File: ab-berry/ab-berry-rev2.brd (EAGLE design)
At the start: 58.4 x 61 mm, 66 parts, among them IC1 STM32F302RCT6, U1 LM1117MPX-3.3/NOPB or AP2114H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

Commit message: wip
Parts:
- removed STM32F072CBT6: STM32F072-LQFP48, stm32f0:LQFP48
- added R23, R24: 22, microbuilder:0603
- added X1: (no value), keves:TE-292304-1
- moved IC1 46.0 mm to (14.7, 33.4), flipped to the bottom
- moved C22 45.4 mm to (6.86, 29.8), flipped to the bottom, turned to 90 degrees
- moved R5 34.8 mm to (-9.14, 52.3)
- moved LED1 34.7 mm to (-9.02, 48.5)
- moved LED2 29.6 mm to (-7.37, 17.3)
- moved R6 29.1 mm to (-9.40, 13.1)
- moved R1 28.9 mm to (-10.8, 33.4)
- moved JP3 26.2 mm to (55.1, 50.0), turned to 90 degrees
- moved C12 15.3 mm to (18.4, 19.7), turned to 180 degrees
- moved C1 15.2 mm to (22.7, 30.1), turned to 90 degrees
- moved C13 14.1 mm to (14.9, 19.7), turned to 180 degrees
- moved C3 13.1 mm to (7.24, 39.0), turned to 270 degrees
- moved C6 11.9 mm to (21.0, 26.9)
- moved C5 10.8 mm to (10.3, 23.2), turned to 0 degrees
- moved U$36 10.5 mm to (16.6, 22.6), turned to 180 degrees
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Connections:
- new net N$18: R23.2, X1.2
- new net N$19: R24.2, X1.3
- new net SPI1_SCK: IC1.55, LCD2.CLK
- new net USB_DM: IC1.44, R23.1
- new net USB_DP: IC1.45, R24.1
- net 5.0V: now also X1.1
- net BTN_USR: now also IC1.2; no longer STM32F072CBT6.2
- net CAN_RX: now also IC1.61; no longer STM32F072CBT6.32
- net CAN_TX: now also IC1.62; no longer STM32F072CBT6.33
- net DBG_RX: no longer STM32F072CBT6.31
- net DBG_TX: no longer STM32F072CBT6.30
- net GND: now also X1.4
- net LCD_CS1: now also IC1.52; no longer STM32F072CBT6.20
- net LCD_CS2: now also IC1.53; no longer STM32F072CBT6.19
- net LCD_DC: now also IC1.59; no longer STM32F072CBT6.14
- net LCD_RST: now also IC1.58; no longer STM32F072CBT6.13
- net N$6: no longer STM32F072CBT6.18
- net N$8: now also IC1.5; no longer STM32F072CBT6.5
- net N$9: now also IC1.6; no longer STM32F072CBT6.6
- net ROT1_A: no longer STM32F072CBT6.27
- net ROT1_B: no longer STM32F072CBT6.28
- net ROT1_SW: no longer STM32F072CBT6.25
- net ROT2_A: no longer STM32F072CBT6.40
- net ROT2_B: no longer STM32F072CBT6.41
- net ROT2_SW: no longer STM32F072CBT6.39
- net ROT3_A: no longer STM32F072CBT6.43
- net ROT3_B: no longer STM32F072CBT6.45
- net ROT3_SW: no longer STM32F072CBT6.42
- net ROT4_A: no longer STM32F072CBT6.26
- net ROT4_B: no longer STM32F072CBT6.22
- net ROT4_SW: no longer STM32F072CBT6.21
- net SPI1_CLK: no longer LCD2.CLK, STM32F072CBT6.15
- net SPI1_MOSI: now also IC1.57; no longer STM32F072CBT6.17
- net SWCLK: no longer STM32F072CBT6.37
- net SWDIO: no longer STM32F072CBT6.34
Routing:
- net ROT4_A: track 54.1 -> 2.30 mm, vias 4 -> 0
- net ROT3_SW: track 46.7 -> 0.00 mm, vias 1 -> 0
- net SPI1_CLK: track 45.8 -> 0.00 mm, vias 1 -> 0
- net ROT3_B: track 44.7 -> 1.98 mm, vias 2 -> 0
- net ROT1_B: track 37.2 -> 2.12 mm, vias 4 -> 0
- net ROT1_A: track 35.3 -> 2.04 mm, vias 4 -> 0
- net ROT3_A: track 34.2 -> 1.98 mm, vias 2 -> 0
- net ROT2_SW: track 27.5 -> 0.00 mm, vias 1 -> 0
- net DBG_TX: track 24.8 -> 0.00 mm, vias 2 -> 0
- net DBG_RX: track 24.5 -> 0.00 mm, vias 2 -> 0
- net ROT1_SW: track 19.6 -> 0.00 mm, vias 3 -> 0
- net ROT4_B: track 54.2 -> 35.6 mm
- net ROT4_SW: track 41.3 -> 23.4 mm
- net LCD_CS1: track 48.5 -> 31.3 mm
- net SWDIO: track 16.8 -> 0.00 mm
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
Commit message: wip
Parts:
- moved R5 60.2 mm to (49.5, 39.0)
- moved LED1 60.0 mm to (49.5, 35.3)
- moved R1 35.6 mm to (24.6, 29.8), turned to 90 degrees
- moved R6 30.5 mm to (5.84, 39.5), turned to 180 degrees
- moved LED2 24.3 mm to (2.41, 39.5), turned to 270 degrees
- moved C3 1.80 mm to (5.97, 37.7), turned to 180 degrees
- moved C1 1.42 mm to (22.5, 28.7)
- moved C6 1.14 mm to (20.4, 25.9)
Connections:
- net DBG_RX: now also IC1.30
- net DBG_TX: now also IC1.29
- net N$6: now also IC1.33
- net ROT1_A: now also IC1.16
- net ROT1_B: now also IC1.15
- net ROT1_SW: now also IC1.14
- net ROT2_A: now also IC1.38
- net ROT2_B: now also IC1.40
- net ROT2_SW: now also IC1.39
- net ROT3_A: now also IC1.42
- net ROT3_B: now also IC1.43
- net ROT3_SW: now also IC1.41
- net ROT4_A: now also IC1.10
- net ROT4_B: now also IC1.9
- net ROT4_SW: now also IC1.8

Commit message: wip
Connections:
- removed net SPI1_CLK: LCD1.CLK
- net SPI1_SCK: now also LCD1.CLK
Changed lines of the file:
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@@
 <wire x1="20.482" y1="32.651" x2="26.84" y2="27.94" width="0" layer="19" extent="16-16"/>
-</signal>
-<signal name="SPI1_CLK">
-<contactref element="LCD1" pad="CLK"/>
 </signal>
 <signal name="LCD_CS2">
@@
 <contactref element="IC1" pad="55"/>
 <contactref element="LCD2" pad="CLK"/>
+<contactref element="LCD1" pad="CLK"/>
+<wire x1="26.84" y1="33.02" x2="56.304" y2="33.02" width="0" layer="19" extent="1-1"/>
 <wire x1="20.482" y1="34.151" x2="26.84" y2="33.02" width="0" layer="19" extent="16-16"/>
 </signal>

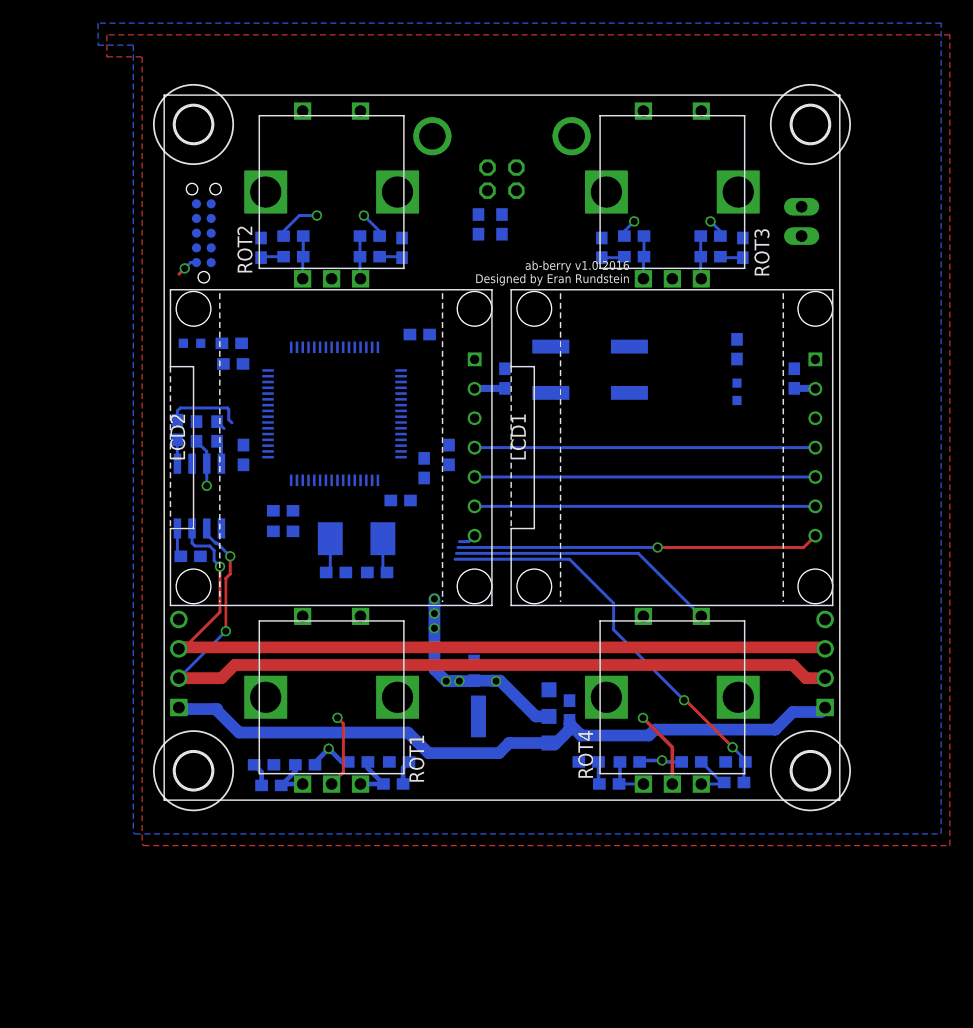
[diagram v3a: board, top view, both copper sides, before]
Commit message: switch ab-berry-rev2 to STM32F303CCT6
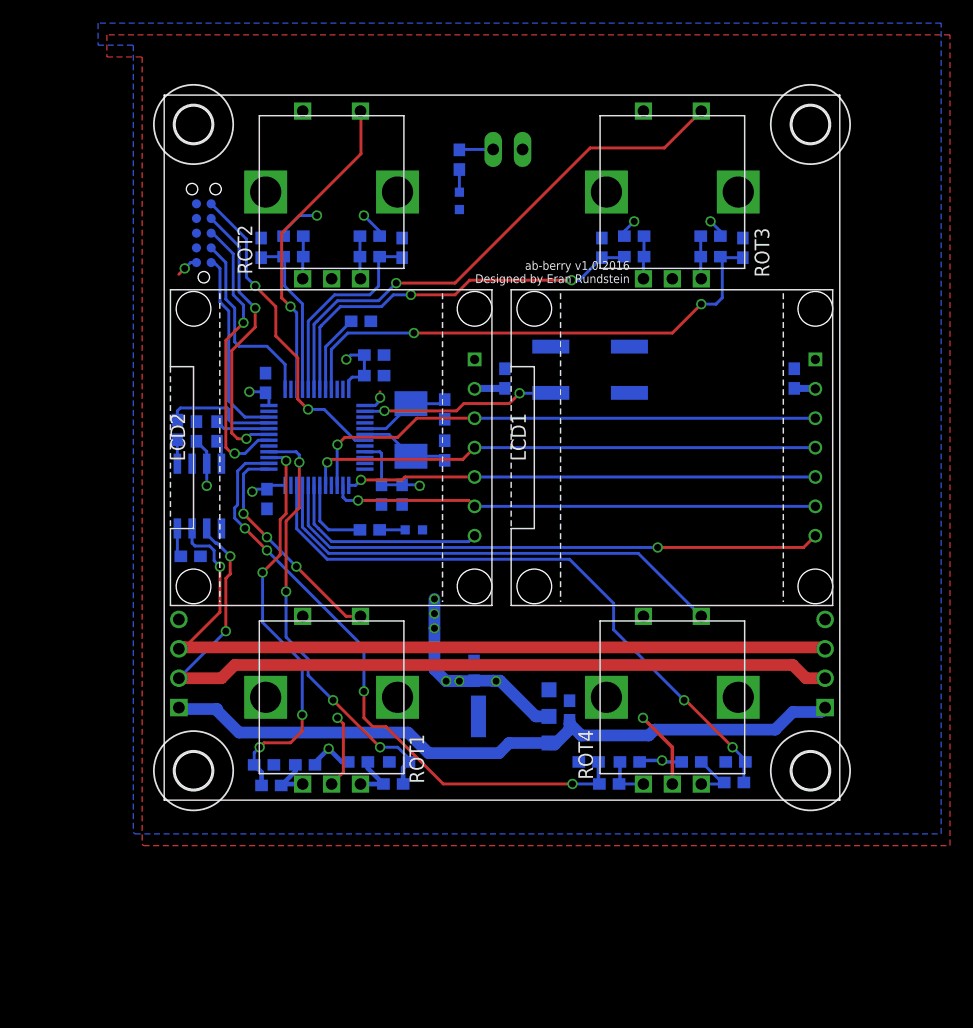
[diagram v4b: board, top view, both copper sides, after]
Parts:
- removed C22: 0.1uF, microbuilder:0603
- removed R23, R24: 22, microbuilder:0603
- removed X1: (no value), keves:TE-292304-1
- IC1: value STM32F302RCT6 -> STM32F302_F303_B_C_LQFP48; device keves:TQFP64 -> keves:TQFP48
- moved LED1 29.1 mm to (25.5, 51.8)
- moved R5 29.1 mm to (25.5, 55.4)
- moved JP3 26.2 mm to (29.7, 56.3), turned to 180 degrees
- moved LED2 25.1 mm to (21.6, 23.4), turned to 90 degrees
- moved R6 20.1 mm to (17.8, 23.4), turned to 0 degrees
- moved C1 15.6 mm to (8.76, 36.1), turned to 270 degrees
- moved C12 15.3 mm to (24.3, 33.8), turned to 90 degrees
- moved C13 14.1 mm to (24.3, 30.2), turned to 90 degrees
- moved R1 13.8 mm to (17.0, 41.4), turned to 0 degrees
- moved C6 12.8 mm to (18.2, 38.5)
- moved C3 12.0 mm to (8.89, 26.0), turned to 90 degrees
- moved C5 10.8 mm to (20.6, 26.4), turned to 270 degrees
- moved U$36 10.5 mm to (21.3, 32.0), turned to 90 degrees
- moved C4 8.62 mm to (18.8, 26.4), turned to 90 degrees
- moved C2 5.31 mm to (18.2, 36.7)
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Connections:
- net NRST renamed RST
- removed net N$18: R23.2, X1.2
- removed net N$19: R24.2, X1.3
- removed net SPI1_SCK: IC1.55, LCD1.CLK, LCD2.CLK
- removed net USB_DM: IC1.44, R23.1
- removed net USB_DP: IC1.45, R24.1
- new net SPI1_CLK: IC1.15, LCD1.CLK, LCD2.CLK
- net 3.3V: now also IC1.24, IC1.36, IC1.9; no longer C22.2, IC1.13, IC1.19, IC1.32, IC1.64
- net 5.0V: no longer X1.1
- net CAN_RX: now also IC1.32; no longer IC1.61
- net CAN_TX: now also IC1.33; no longer IC1.62
- net DBG_RX: now also IC1.31; no longer IC1.30
- net DBG_TX: now also IC1.30; no longer IC1.29
- net GND: now also IC1.23, IC1.35, IC1.8; no longer C22.1, IC1.12, IC1.31, IC1.63, X1.4
- net LCD_CS1: now also IC1.20; no longer IC1.52
- net LCD_CS2: now also IC1.19; no longer IC1.53
- net LCD_DC: now also IC1.14; no longer IC1.59
- net LCD_RST: now also IC1.13; no longer IC1.58
- net N$1: now also IC1.44; no longer IC1.60
- net N$6: now also IC1.18; no longer IC1.33
- net ROT1_A: now also IC1.27; no longer IC1.16
- net ROT1_B: now also IC1.28; no longer IC1.15
- net ROT1_SW: now also IC1.25; no longer IC1.14
- net ROT2_A: now also IC1.40; no longer IC1.38
- net ROT2_B: now also IC1.41; no longer IC1.40
- net ROT3_A: now also IC1.43; no longer IC1.42
- net ROT3_B: now also IC1.45; no longer IC1.43
- net ROT3_SW: now also IC1.42; no longer IC1.41
- net ROT4_A: now also IC1.26; no longer IC1.10
- net ROT4_B: now also IC1.22; no longer IC1.9
- net ROT4_SW: now also IC1.21; no longer IC1.8
- net SPI1_MOSI: now also IC1.17; no longer IC1.57
- net SWCLK: now also IC1.37; no longer IC1.49
- net SWDIO: now also IC1.34; no longer IC1.46
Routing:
- net ROT4_A: track 2.30 -> 54.1 mm, vias 0 -> 4
- net ROT3_SW: track 0.00 -> 46.7 mm, vias 0 -> 1
- net SPI1_CLK: track 0.00 -> 45.8 mm, vias 0 -> 1
- net ROT3_B: track 1.98 -> 44.7 mm, vias 0 -> 2
- net ROT1_B: track 2.12 -> 37.2 mm, vias 0 -> 4
- net ROT1_A: track 2.04 -> 35.3 mm, vias 0 -> 4
- net ROT3_A: track 1.98 -> 34.2 mm, vias 0 -> 2
- net ROT2_SW: track 0.00 -> 27.5 mm, vias 0 -> 1
- net RST: track 0.00 -> 27.3 mm, vias 0 -> 2
- net 3.3V: track 48.9 -> 74.2 mm, vias 14 -> 19
- net DBG_TX: track 0.00 -> 24.8 mm, vias 0 -> 2
- net DBG_RX: track 0.00 -> 24.5 mm, vias 0 -> 2
- net ROT1_SW: track 0.00 -> 19.6 mm, vias 0 -> 3
- net ROT4_B: track 35.6 -> 54.2 mm
- net ROT4_SW: track 23.4 -> 41.3 mm
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
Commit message: wip
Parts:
- added C22: 4.7nF, microbuilder:0603
- added R23, R24: 22, microbuilder:0603
- added R25: 1M, microbuilder:0603
- added U2: PRTR5V0U2X, Volks73-NXPSemiconductors:SOT-143B
- added X1: (no value), keves:TE-292304-1
- IC1: value STM32F302_F303_B_C_LQFP48 -> STM32F303CCT6
- LCD1, LCD2: value SSD1306-7PIN -> SSD1306-7PINWITHOUT-HOLES; device keves:SSD1306-7PIN -> keves:SSD1306-7PIN-NO-HOLES
- moved R5 29.8 mm to (50.7, 39.4)
- moved JP3 26.5 mm to (55.6, 50.5), turned to 90 degrees
- moved LED1 25.9 mm to (48.1, 39.2), turned to 0 degrees
- moved C8 5.22 mm to (33.4, 2.79), turned to 90 degrees
- moved R19 2.88 mm to (38.5, 45.1)
- moved R21 2.80 mm to (38.5, 47.0)
- moved C20 2.70 mm to (35.8, 46.0)
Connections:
- removed net N$6: IC1.18, R6.2
- new net N$18: R23.1, U2.3, X1.2
- new net N$19: R24.1, U2.2, X1.3
- new net N$20: C22.1, R25.1, X1.P$1, X1.P$2
- new net USB_DM: IC1.32, R23.2
- new net USB_DP: IC1.33, R24.2
- net 5.0V: now also U2.4, X1.1
- net CAN_RX: now also IC1.45; no longer IC1.32
- net CAN_TX: now also IC1.46; no longer IC1.33
- net GND: now also C22.2, R25.2, U2.1, X1.4
- net ROT3_B: no longer IC1.45
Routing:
- net 5.0V: track 60.7 -> 122.2 mm, vias 0 -> 4
- net N$18: track 0.00 -> 50.5 mm
- net N$19: track 0.00 -> 49.3 mm
- net N$20: track 0.00 -> 21.8 mm
- net USB_DM: track 0.00 -> 12.7 mm
- net USB_DP: track 0.00 -> 11.6 mm
- net CAN_RX: track 4.74 -> 15.3 mm, vias 0 -> 2
- net CAN_TX: track 9.88 -> 17.5 mm, vias 0 -> 2
- net N$6: track 6.87 -> 0.00 mm
- net ROT3_SW: track 46.7 -> 52.0 mm, vias 1 -> 2
- net ROT3_B: track 44.7 -> 41.3 mm, vias 2 -> 4
- net GND: track 13.1 -> 16.5 mm
- net ROT3_A: track 34.2 -> 31.3 mm
- net N$16: track 3.71 -> 1.93 mm
- net 3.3V: track 74.2 -> 75.9 mm, vias 19 -> 20
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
